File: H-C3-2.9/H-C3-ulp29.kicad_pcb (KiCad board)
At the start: 4 copper layers, 81.5 x 47.5 mm, 67 parts, among them IC101 ESP32-C3-WROOM-02-H4, J1 USB_C_Receptacle_USB2.0, J2 AFC24-S24FIC-00, J3 SM02B-SRSS-TB(LF)(SN), J4 SM04B-SRSS-TB_LF__SN_, J5 OLED, Q1 Si1308, Q2 Si2301CDS, SW1 SW_Push_Dual, SW2 SW_Push_Dual, U2 SGM6029CYG/TR, U3 TP4057-42-SOT26-R, U4 K2-1806SQ-A2DW-04, U5 K2-1806SQ-A2DW-04, U6 K2-1806SQ-A2DW-04, Y1 RV-3032-C7

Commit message: Layout 1.0
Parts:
- removed C2, C3: 10 uF, Capacitor_SMD:C_0603_1608Metric
- removed H1: MountingHole, MountingHole:MountingHole_3.7mm
- removed J5: OLED, Connector_PinSocket_2.54mm:PinSocket_1x04_P2.54mm_Vertical
- removed L2: 0.47 uH, footprints:IND-SMD_L2.5-W2.0_SPH252012
- removed R3: 249k 1%, Resistor_SMD:R_0603_1608Metric
- removed TP10: RX, TestPoint:TestPoint_Pad_D1.0mm
- removed TP9: TX, TestPoint:TestPoint_Pad_D1.0mm
- removed U2: SGM6029CYG/TR, footprints:SGM6029_WLCSP-6
- removed Y1: RV-3032-C7, footprints:RV3032C7
- moved U6 4.21 mm to (88.9, 77.5), turned to 90 degrees
- moved J4 3.45 mm to (159.0, 44.8)
- moved R21 3.34 mm to (91.7, 78.8)
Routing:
- net VDD33: track 51.6 -> 13.2 mm, vias 6 -> 3
- net /SCL: track 38.4 -> 0.00 mm
- net BOOT: track 49.2 -> 12.8 mm, vias 2 -> 1
- net /SDA: track 33.3 -> 0.00 mm, vias 2 -> 0
- net /IO_22: track 20.6 -> 1.61 mm
- net /RTC_SQW: track 18.9 -> 0.00 mm, vias 1 -> 0
- net +3V3: track 36.4 -> 17.9 mm, vias 7 -> 4
- net /IO_23: track 19.3 -> 1.10 mm
- net VDD_RTC: track 16.4 -> 0.00 mm, vias 1 -> 0
- net /IO_21: track 17.3 -> 0.95 mm
- net VDD: track 24.4 -> 9.75 mm
- net GND: track 78.4 -> 65.1 mm, vias 41 -> 24
- net /IO_RX: track 10.9 -> 0.00 mm, vias 1 -> 0
- net /IO_TX: track 9.88 -> 0.00 mm, vias 1 -> 0
- net (no net): track 27.8 -> 22.7 mm, vias 2 -> 1
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- removed copper zone on B.Cu, net GND
- removed copper zone on F.Cu, net GND
- removed copper zone on In2.Cu, net VDD33
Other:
- board size 81.5 x 47.5 mm -> 83.4 x 42.1 mm
- board text added: "RESET"
- board text added: "github.com/martinberlin/H-C3-029-eink"
- board text removed: "0 1 2 3 4 5 6 7"
- board text removed: "1.1"
- board text removed: "16"
- board text removed: "17"
- board text removed: "3V3"
- board text removed: "C6"
- board text removed: "GND"
- board text removed: "Mini TFT I2C"
- board text removed: "RTC"
- board text removed: "SCL"
- board text removed: "SDA"
- board text removed: "ULP"
- board text removed: "github.com/martinberlin/H-C6-ulp"

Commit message: Schematics updated. All parts on board
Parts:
- removed C1: 1uF, Capacitor_SMD:C_0402_1005Metric
- removed C23: 22pF, Capacitor_SMD:C_0402_1005Metric
- removed C24: superCAP, footprints:superCAP-XH414HG
- removed D4: RED, LED_SMD:LED_0805_2012Metric
- removed D6: GRE, LED_SMD:LED_0805_2012Metric
- removed IC101: ESP32-C3-WROOM-02-H4, footprints:ESP32C3WROOM02H4
- removed J3: SM02B-SRSS-TB(LF)(SN), footprints:SM02BSRSSTBLFSN
- removed R11, R13: 5.1k, Resistor_SMD:R_0603_1608Metric
- removed R12: 2K2, Resistor_SMD:R_0805_2012Metric
- removed R16, R17: 10k, Resistor_SMD:R_0402_1005Metric
- removed TP7: 22, TestPoint:TestPoint_Pad_D1.0mm
- removed TP8: 23, TestPoint:TestPoint_Pad_D1.0mm
- removed U3: TP4057-42-SOT26-R, footprints:TP4057-42-SOT26-R
- removed U4, U5, U6: K2-1806SQ-A2DW-04, footprints:KEY-SMD_K2-1806SQ-A3DW-04
- added BT1: Battery_Cell, footprints:BAT-SMD_BS-24-B4AA016, F.Cu at (127.1, 53.0)
- added C19: C_Polarized 100uF, Capacitor_Tantalum_SMD:CP_EIA-3528-21_Kemet-B, F.Cu at (119.7, 71.0)
- added C2: 22pF, Capacitor_SMD:C_0402_1005Metric, F.Cu at (90.6, 76.2)
- added C20: 12 pF, Capacitor_SMD:C_0603_1608Metric, F.Cu at (110.4, 71.8)
- added C21: 12 pF, Capacitor_SMD:C_0603_1608Metric, F.Cu at (110.4, 79.3)
- added D8: 1N4148WS, Diode_SMD:D_SOD-323, F.Cu at (115.4, 70.4)
- added IC1: ESP32-C3-WROOM-02-H4, footprints:ESP32C3WROOM02H4, F.Cu at (107.2, 72.5)
- added R18: 10 K, Resistor_SMD:R_0603_1608Metric, F.Cu at (110.4, 70.1)
- added R3: 10k, Resistor_SMD:R_0402_1005Metric, F.Cu at (164.9, 70.8)
- added R4: 10k, Resistor_SMD:R_0402_1005Metric, F.Cu at (90.6, 78.7)
- added SW3: K2-1806SQ-A2DW-04, footprints:KEY-SMD_K2-1806SQ-A3DW-04, F.Cu at (167.6, 49.3)
- added U8: PCF8563T, Package_SO:SOIC-8_3.9x4.9mm_P1.27mm, F.Cu at (115.7, 75.8)
- added Y1: Crystal_Small, footprints:Q13FC1350000400-Crystal, F.Cu at (108.2, 76.2)
- SW1, SW2: value SW_Push_Dual -> K2-1806SQ-A2DW-04; footprint footprints:switch_SKSVCCE010 -> footprints:KEY-SMD_K2-1806SQ-A3DW-04
- TP6: value 21 -> IO8
- moved R21 79.2 mm to (164.8, 48.2)
- moved R2 57.3 mm to (90.9, 47.9)
- moved SW2 38.4 mm to (87.9, 49.2), turned to 90 degrees
- moved SW1 34.9 mm to (87.9, 77.4), turned to 90 degrees
- moved TP6 20.1 mm to (103.4, 79.0)
- moved R10 13.4 mm to (136.4, 66.3), turned to 45 degrees
- moved Q2 8.78 mm to (135.1, 69.3)
- moved R20 7.01 mm to (130.5, 70.0), turned to 45 degrees
- moved D5 5.35 mm to (133.2, 66.8), turned to -135 degrees
- moved R1 5.30 mm to (124.1, 70.1)
- moved J1 4.23 mm to (127.7, 77.4)
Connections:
- C9 pad 2: VDD33 -> +3V3
- D5 pad 1: VDD -> +3V3
- J2 pad 10: VDD33 -> +3V3
- J2 pad 9: VDD33 -> +3V3
- J4 pad 1: /SCL -> GND
- J4 pad 2: /SDA -> +3V3
- J4 pad 3: +3V3 -> /SDA
- J4 pad 4: GND -> /SCL
- Q2 pad 2: VDD -> +3V3
- Q2 pad 3: VBAT -> +VBAT
- SW1 pad 1: SW10 -> BOOT
- SW1 pad 3: SW10 -> unconnected-(SW1-Pad3)
- SW1 pad 4: GND -> unconnected-(SW1-Pad4)
- SW2 pad 1: BOOT -> SW10
- SW2 pad 3: BOOT -> unconnected-(SW2-Pad3)
- SW2 pad 4: GND -> unconnected-(SW2-Pad4)
- TP6 pad 1: /IO_21 -> Net-(IC1-IO8)
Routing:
- net VBUS: track 47.0 -> 8.73 mm, vias 2 -> 0
- net GND: track 65.1 -> 31.6 mm, vias 24 -> 11
- net SW10: track 31.3 -> 0.00 mm, vias 2 -> 0
- net SW8: track 31.2 -> 0.00 mm
- net VBAT: track 22.8 -> 0.00 mm
- net (no net): track 22.7 -> 0.04 mm, vias 1 -> 0
- net /EPD_RST: track 28.0 -> 13.4 mm, vias 2 -> 0
- net VDD33: track 13.2 -> 0.00 mm, vias 3 -> 0
- net BOOT: track 12.8 -> 0.00 mm, vias 1 -> 0
- net Net-(J1-CC2): track 10.9 -> 0.00 mm, vias 2 -> 0
- net VDD: track 9.75 -> 0.00 mm
- net Net-(D6-K): track 8.71 -> 0.00 mm
- net +3V3: track 17.9 -> 25.3 mm, vias 4 -> 6
- net Net-(U3-*CHRG): track 5.44 -> 0.00 mm
- net Net-(D4-K): track 4.15 -> 0.00 mm
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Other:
- board text added: "BOOT IO9"
- board text added: "IO10"
- board text removed: "+"
- board text removed: "18"
- board text removed: "20"
- board text removed: "21▶"
- board text removed: "22"
- board text removed: "23"
- board text removed: "BOOT"
- board text removed: "CHARGE"
- board text removed: "READY"
- board text removed: "RST"

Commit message: Going forward
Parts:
- removed IC1: ESP32-C3-WROOM-02-H4, footprints:ESP32C3WROOM02H4
- removed TP4: IO20, TestPoint:TestPoint_Pad_D1.0mm
- removed TP5: IO21, TestPoint:TestPoint_Pad_D1.0mm
- removed TP6: IO8, TestPoint:TestPoint_Pad_D1.0mm
- added C1: 1uF, Capacitor_SMD:C_0402_1005Metric, F.Cu at (90.8, 50.5)
- added C3: 1uF, Capacitor_SMD:C_0805_2012Metric, F.Cu at (108.3, 58.0)
- added C4: 1uF, Capacitor_SMD:C_0805_2012Metric, F.Cu at (108.3, 63.9)
- added C5: 100nF, Capacitor_SMD:C_0805_2012Metric, F.Cu at (106.2, 49.5)
- added U1: E104-BT5032A, footprints:nRF52832_E104-BT5032A_BYT, F.Cu at (94.5, 62.0)
- added U2: XC6206PxxxMR, Package_TO_SOT_SMD:SOT-23-3, F.Cu at (111.3, 61.0)
- added U3: CH340C, Package_SO:SOIC-16_3.9x9.9mm_P1.27mm, F.Cu at (99.8, 49.3)
- moved R14 3.20 mm to (144.1, 62.0)
- moved R15 3.20 mm to (142.5, 62.0)
- moved BT1 1.09 mm to (127.3, 54.0)
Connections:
- net +VBAT renamed Net-(BT1-+)
- net /ESP_RST renamed /MCU_RST
- net SW10 renamed SW2
- net VBUS renamed +5V
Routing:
- net +3V3: track 25.3 -> 23.6 mm, vias 6 -> 4

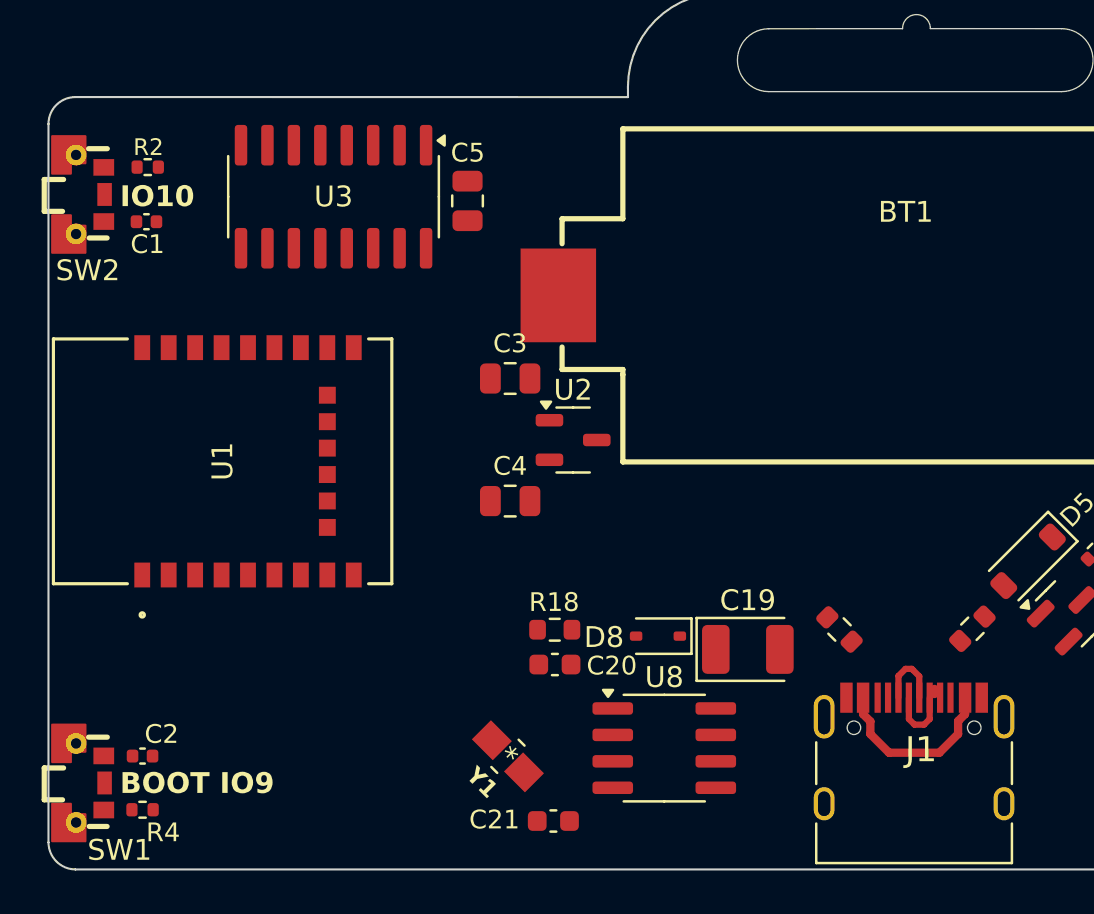
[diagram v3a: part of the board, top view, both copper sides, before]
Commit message: Final decision about MCU
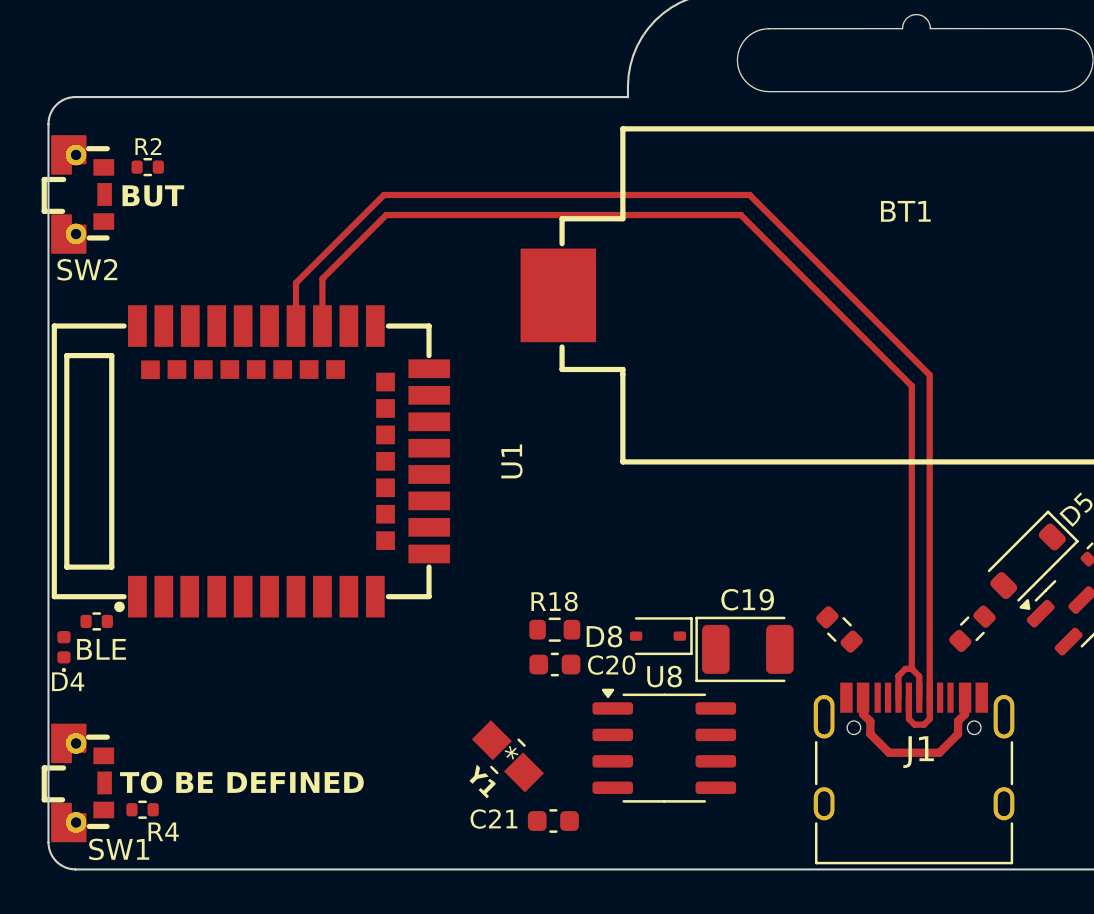
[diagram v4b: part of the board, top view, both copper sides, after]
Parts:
- removed C1: 1uF, Capacitor_SMD:C_0402_1005Metric
- removed C2: 22pF, Capacitor_SMD:C_0402_1005Metric
- removed C3, C4: 1uF, Capacitor_SMD:C_0805_2012Metric
- removed C5: 100nF, Capacitor_SMD:C_0805_2012Metric
- removed U2: XC6206PxxxMR, Package_TO_SOT_SMD:SOT-23-3
- removed U3: CH340C, Package_SO:SOIC-16_3.9x9.9mm_P1.27mm
- added D4: LED, LED_SMD:LED_0402_1005Metric, F.Cu at (86.8, 70.9)
- added R5: 3.3k, Resistor_SMD:R_0402_1005Metric, F.Cu at (88.4, 69.7)
- U1: value E104-BT5032A -> E73-2G4M08S1C; footprint footprints:nRF52832_E104-BT5032A_BYT -> footprints:C356849-nRF52840
- moved U1 2.92 mm to (97.4, 62.0), turned to -90 degrees
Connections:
- R2 pad 1: SW2 -> GND
- R2 pad 2: +3V3 -> Net-(R2-Pad2)
- R4 pad 1: BOOT -> GND
- R4 pad 2: +3V3 -> Net-(R4-Pad2)
- SW1 pad 1: BOOT -> SW1
- SW1 pad 2: GND -> Net-(R4-Pad2)
- SW2 pad 2: GND -> Net-(R2-Pad2)
- U1 pad 1: GND -> unconnected-(U1-P1.11-Pad1)
- U1 pad 16: GND -> unconnected-(U1-P0.08-Pad16)
- U1 pad 17: +3V3 -> unconnected-(U1-P1.09-Pad17)
- U1 pad 18: /USB_TXD -> unconnected-(U1-AI2-Pad18)
- U1 pad 19: /USB_RXD -> +3V3
- U1 pad 2: SW2 -> unconnected-(U1-P1.10-Pad2)
- U1 pad 20: /~{RTS} -> unconnected-(U1-P12-Pad20)
- U1 pad 21: /~{CTS} -> GND
- U1 pad 22: unconnected-(U1-P0.21/RST-Pad22) -> /EPD_RST
- U1 pad 24: unconnected-(U1-SWDIO-Pad24) -> GND
- U1 pad 3: unconnected-(U1-P0.26-Pad3) -> /EPD_CLK
- U1 pad 5: unconnected-(U1-WKP-Pad5) -> GND
- U1 pad 9: GND -> unconnected-(U1-AI7-Pad9)
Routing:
- net /USB_D+: track 3.27 -> 56.6 mm
- net /USB_D-: track 3.36 -> 52.2 mm
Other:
- board text added: "BLE"
- board text added: "BUT"
- board text added: "TO BE DEFINED"
- board text removed: "BOOT IO9"
- board text removed: "IO10"

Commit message: Starting to test routing posibilities
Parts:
- added R6: 10k, Resistor_SMD:R_0402_1005Metric, F.Cu at (166.1, 80.2)
- added SW4: K2-1806SQ-A2DW-04, footprints:KEY-SMD_K2-1806SQ-A3DW-04, F.Cu at (167.6, 77.5)
- moved R14 53.2 mm to (92.5, 75.0), turned to 135 degrees
- moved R15 51.3 mm to (92.3, 72.5), turned to 135 degrees
- moved BT1 2.03 mm to (127.2, 56.1)
- moved R3 1.00 mm to (165.9, 70.8)
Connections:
- R5 pad 2: unconnected-(R5-Pad2) -> Net-(U1-P1.13)
- U1 pad 1: unconnected-(U1-P1.11-Pad1) -> /SDA
- U1 pad 16: unconnected-(U1-P0.08-Pad16) -> /EPD_CS
- U1 pad 17: unconnected-(U1-P1.09-Pad17) -> /EPD_MOSI
- U1 pad 2: unconnected-(U1-P1.10-Pad2) -> /SCL
- U1 pad 22: /EPD_RST -> /EPD_CLK
- U1 pad 3: /EPD_CLK -> /EPD_RST
- U1 pad 32: /EPD_BUSY -> unconnected-(U1-P0.20-Pad32)
- U1 pad 33: /EPD_MOSI -> /MCU_BOOT
- U1 pad 34: /EPD_CS -> /EPD_DC
- U1 pad 35: /EPD_DC -> /EPD_BUSY
- U1 pad 6: unconnected-(U1-P1.13-Pad6) -> Net-(U1-P1.13)
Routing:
- net /EPD_RST: track 13.4 -> 99.2 mm
- net /EPD_DC: track 6.60 -> 73.1 mm, vias 0 -> 2
- net /EPD_CLK: track 6.67 -> 62.6 mm
- net /EPD_BUSY: track 15.1 -> 69.6 mm, vias 1 -> 0
- net /EPD_MOSI: track 0.00 -> 53.9 mm
- net /EPD_CS: track 6.92 -> 0.00 mm
- net +3V3: track 23.6 -> 17.3 mm, vias 4 -> 2
- net GND: track 31.3 -> 26.7 mm
- net /USB_D+: track 56.6 -> 52.4 mm, vias 0 -> 2
- net /USB_D-: track 52.2 -> 48.5 mm, vias 0 -> 2

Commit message: Please approve routing
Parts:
- removed R6: 10k, Resistor_SMD:R_0402_1005Metric
- removed SW4: K2-1806SQ-A2DW-04, footprints:KEY-SMD_K2-1806SQ-A3DW-04
- added CN1: HX JN1.27-2X5 TP H4.9, footprints:C42372555-SWD_10P-P1.27, F.Cu at (140.3, 71.9)
- moved D5 8.40 mm to (134.8, 75.0), turned to -90 degrees
- moved BT1 1.16 mm to (127.8, 57.1)
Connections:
- U1 pad 14: unconnected-(U1-P0.06-Pad14) -> /EPD_DC
- U1 pad 33: /MCU_BOOT -> unconnected-(U1-P0.13-Pad33)
- U1 pad 34: /EPD_DC -> unconnected-(U1-P0.22-Pad34)
- U1 pad 37: unconnected-(U1-SWD-Pad37) -> SWDIO
- U1 pad 39: unconnected-(U1-SWC-Pad39) -> SWCLK
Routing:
- net /EPD_CS: track 0.00 -> 57.9 mm, vias 0 -> 2
- net /EPD_DC: track 73.1 -> 58.1 mm
- net Net-(J1-CC1): track 0.00 -> 3.42 mm
- net Net-(J1-CC2): track 0.00 -> 2.92 mm
- added copper zone on In2.Cu, net +3V3

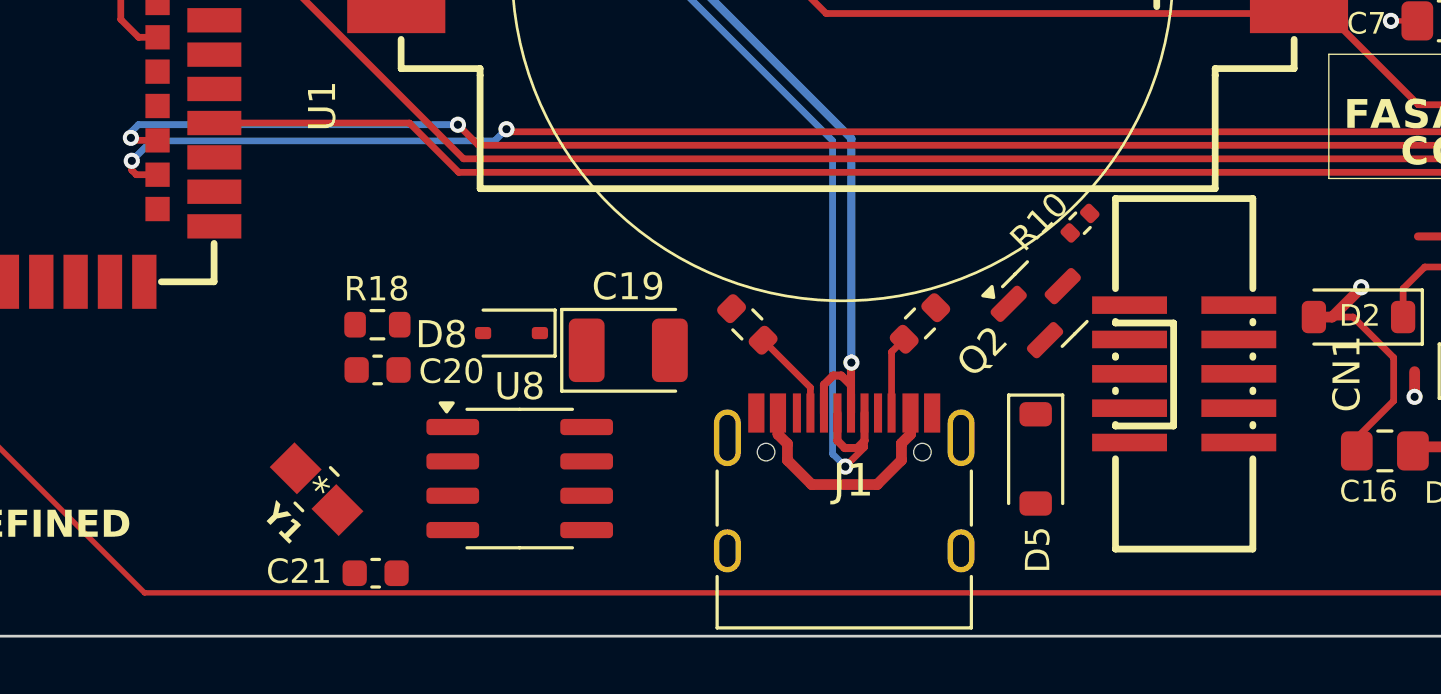
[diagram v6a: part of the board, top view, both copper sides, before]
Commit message: Add nRF52 RTC crystal
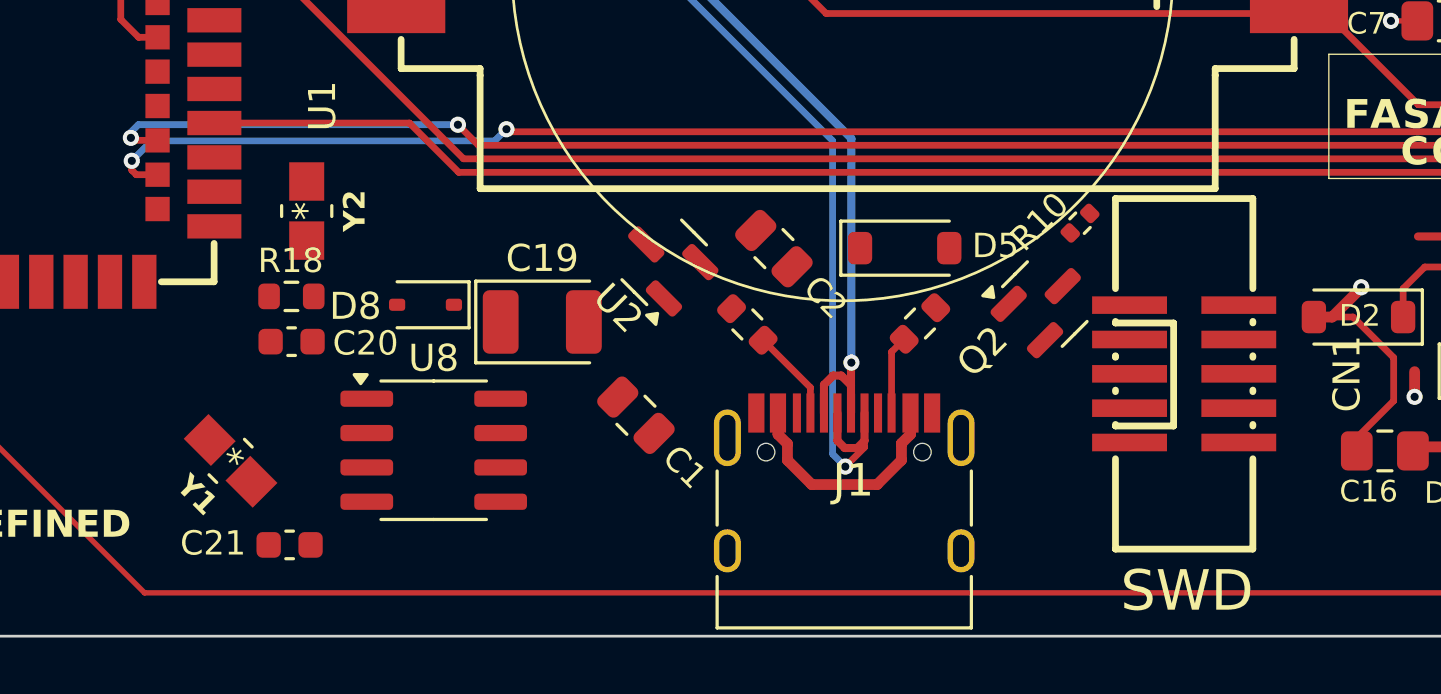
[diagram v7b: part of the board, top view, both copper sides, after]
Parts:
- added C1: 10uF, Capacitor_SMD:C_0805_2012Metric, F.Cu at (120.0, 73.4)
- added C2: 10uF, Capacitor_SMD:C_0805_2012Metric, F.Cu at (125.1, 67.3)
- added U2: MCP1700-3302E_SOT23, Package_TO_SOT_SMD:SOT-23, F.Cu at (121.0, 67.8)
- added Y2: RTC_Crystal_32MHz, footprints:Q13FC1350000400-Crystal, F.Cu at (107.8, 65.9)
- moved D5 9.18 mm to (129.9, 67.3), turned to 0 degrees
- moved U8 3.35 mm to (112.5, 74.7)
- moved Y1 3.35 mm to (105.0, 75.1)
- moved C19 3.35 mm to (116.5, 70.0)
- moved C21 3.35 mm to (107.2, 78.2)
- moved R18 3.35 mm to (107.2, 69.0)
- moved C20 3.35 mm to (107.3, 70.7)
- moved D8 3.35 mm to (112.2, 69.3)
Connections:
- D5 pad 1: +3V3 -> +VIN
- Q2 pad 2: +3V3 -> +VIN
- U1 pad 11: unconnected-(U1-XL1-Pad11) -> Net-(U1-XL1)
- U1 pad 13: unconnected-(U1-XL2-Pad13) -> Net-(U1-XL2)
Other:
- board text added: "SWD"
